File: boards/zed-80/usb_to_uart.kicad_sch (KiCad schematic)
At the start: 11 parts, among them J1 TYPE-C-31-M-12, U1 GD74LS04, U2 CH340C, U6 MC68B50P

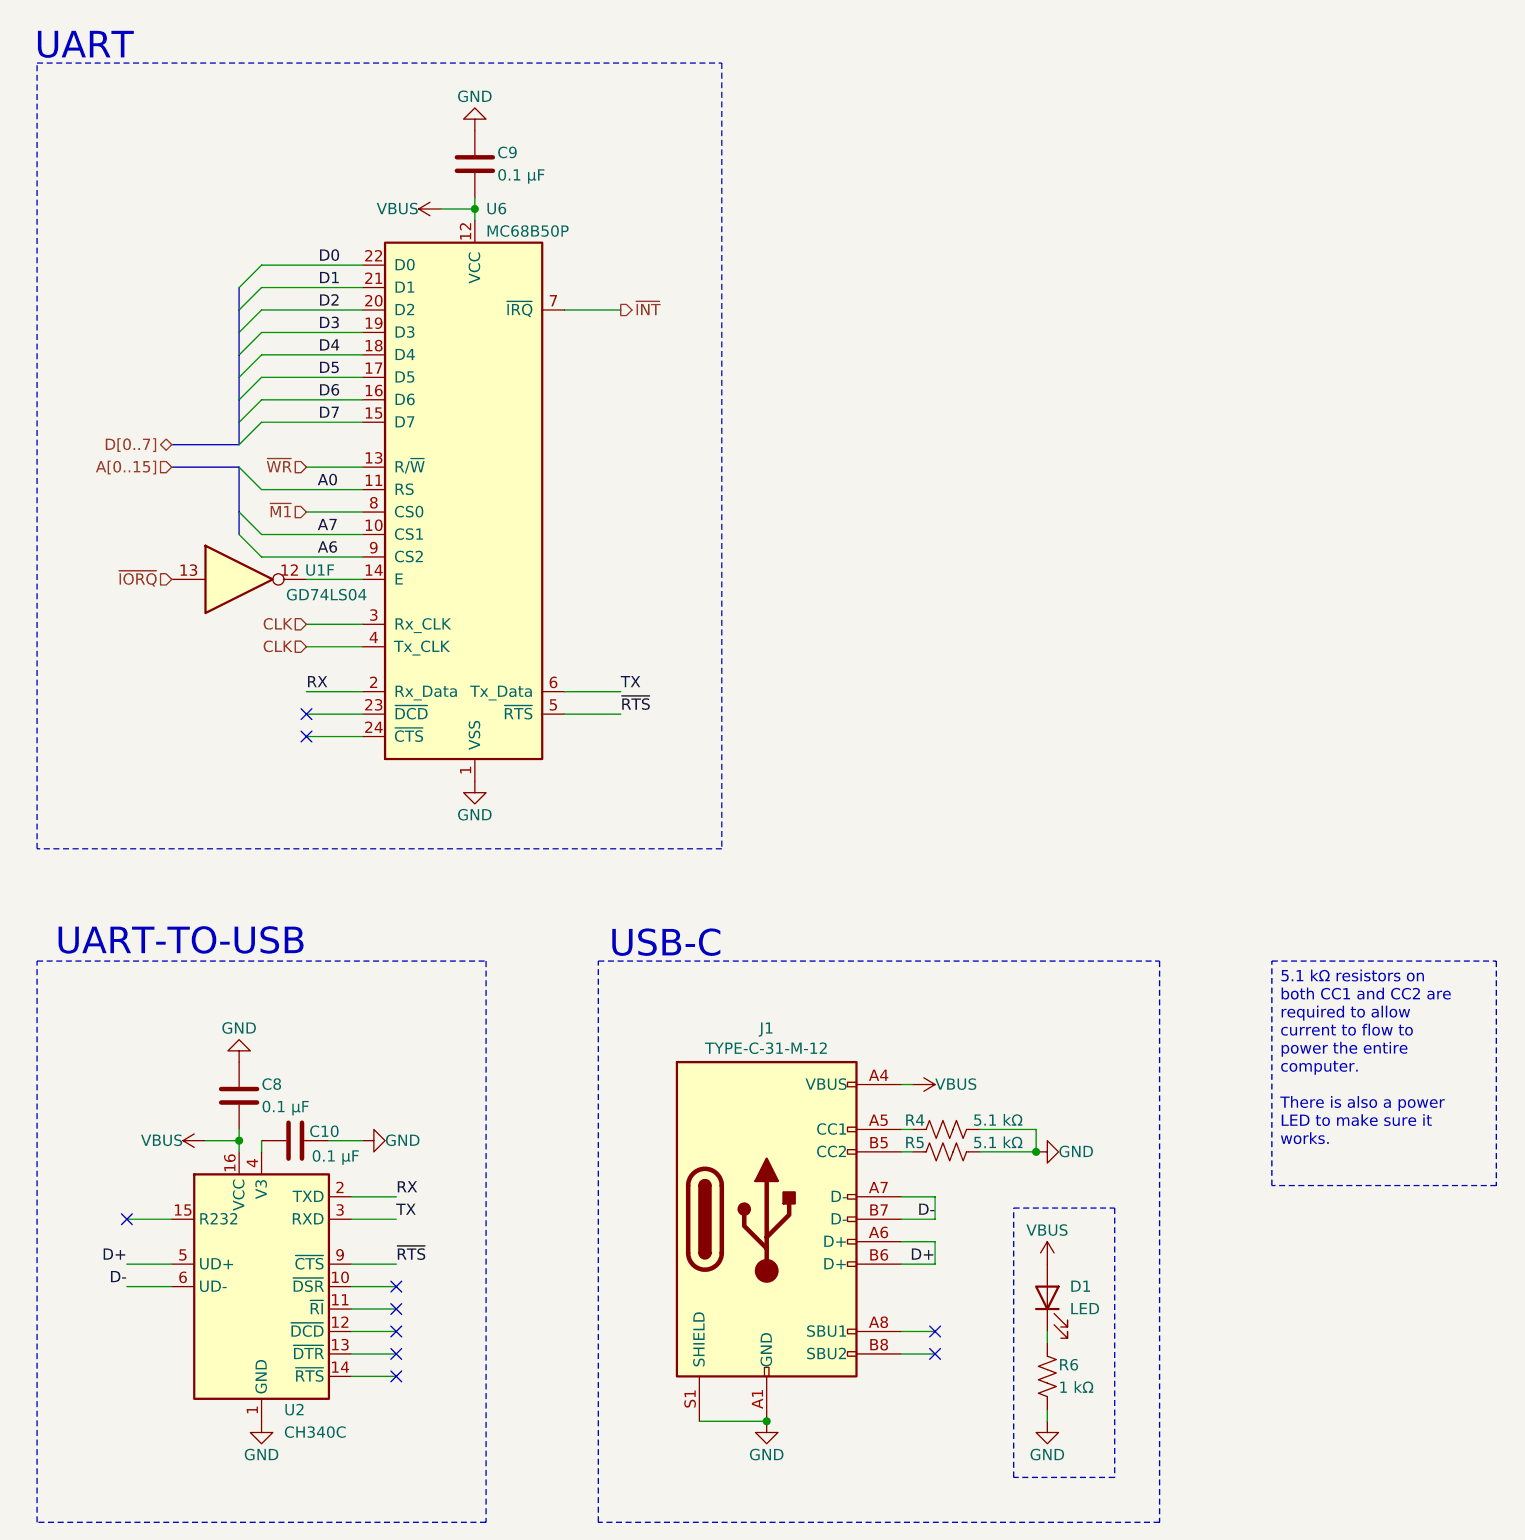
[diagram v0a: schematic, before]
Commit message: Polished schematics and basic PCB setup
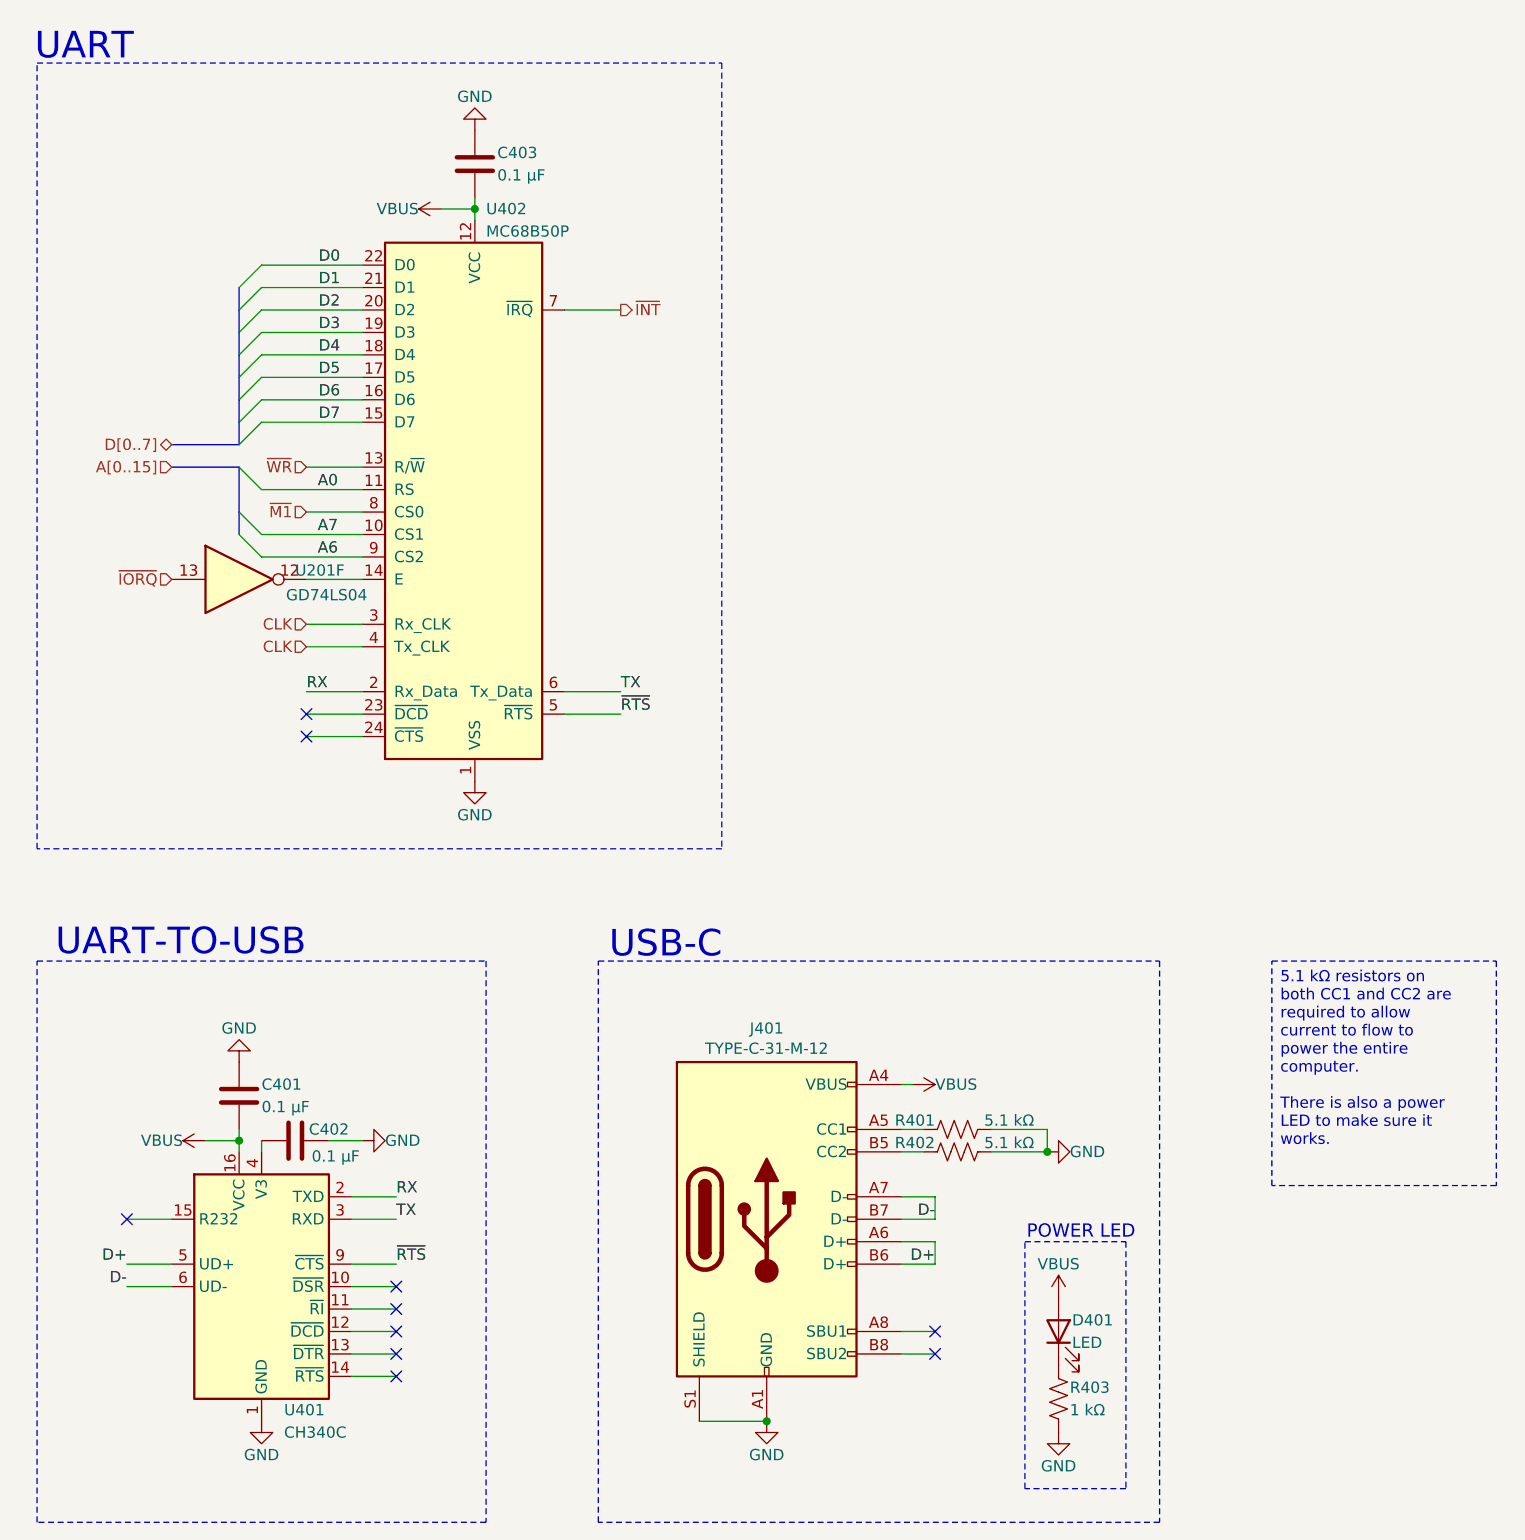
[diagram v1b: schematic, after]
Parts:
- renumbered C8 to C401, C10 to C402, C9 to C403, D1 to D401, J1 to J401, R4 to R401, R5 to R402, R6 to R403, U1 to U201, U2 to U401, U6 to U402
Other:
- note added: "POWER LED"
- company: (none) -> Dragos Bajanica
- title: (none) -> USB-to-UART
- moved on the sheet: D401, R401, R402, R403

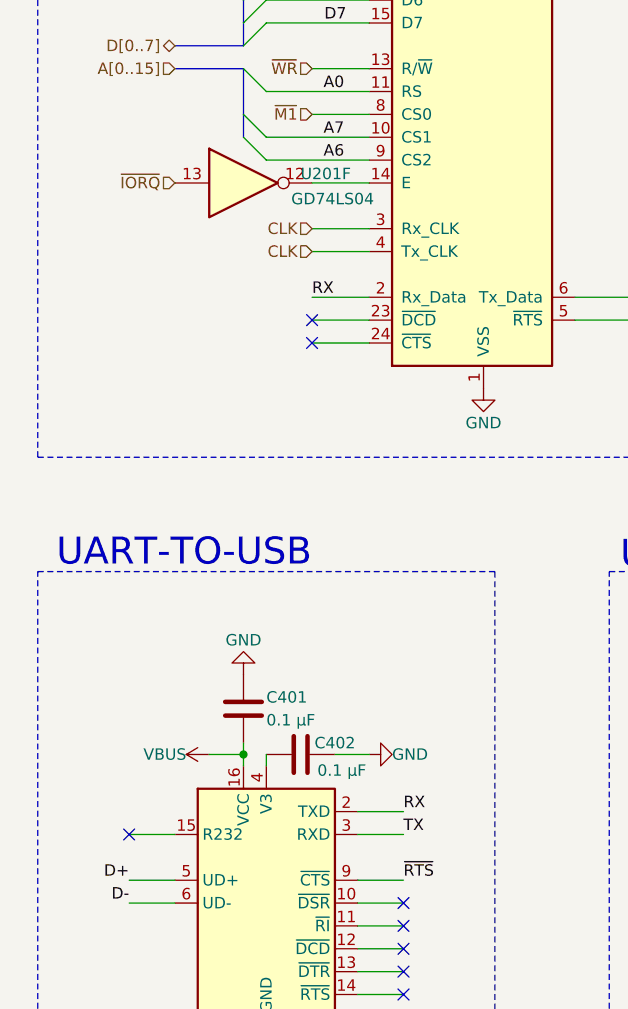
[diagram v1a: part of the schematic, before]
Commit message: New zed-80 revision and initial ROM programmer schematic
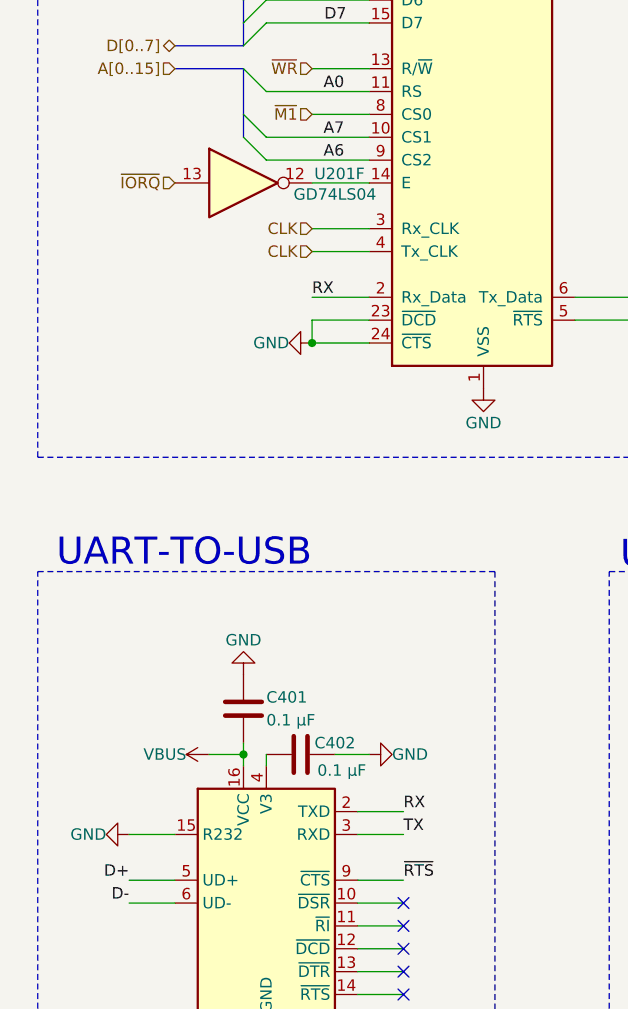
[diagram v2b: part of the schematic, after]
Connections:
- net GND: now also U401.15 (R232), U402.23 (~{DCD}), U402.24 (~{CTS})
- no-connect marks 10 -> 7
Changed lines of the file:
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@@
 	(title_block
 		(title "USB-to-UART")
-		(date "2025-12-31")
-		(rev "A")
+		(date "2026-01-01")
+		(rev "B")
 		(company "Dragos Bajanica")
 	)
@@
 	)
 	(junction
+		(at 55.88 101.6)
+		(diameter 0)
+		(color 0 0 0 0)
+	)
+	(junction
 		(at 107.95 179.07)
 		(diameter 0)
@@
 	)
 	(no_connect
-		(at 55.88 99.06)
-	)
-	(no_connect
 		(at 66.04 168.91)
 	)
@@
 	)
 	(no_connect
-		(at 35.56 156.21)
-	)
-	(no_connect
 		(at 66.04 166.37)
-	)
-	(no_connect
-		(at 55.88 101.6)
 	)
 	(no_connect
@@
 		)
 	)
+	(wire
+		(pts
+			(xy 55.88 99.06) (xy 55.88 101.6)
+		)
+		(stroke
+			(width 0)
+			(type default)
+		)
+	)
 	(bus
 		(pts
@@
 			)
 			(justify left)
+		)
+	)
+	(symbol
+		(lib_id "power:GND")
+		(at 55.88 101.6 270)
+		(mirror x)
+		(unit 1)
+		(exclude_from_sim no)
+		(in_bom yes)
+		(on_board yes)
+		(dnp no)
+		(property "Reference" "#PWR0405"
+			(at 49.53 101.6 0)
+			(effects
+				(font
+					(size 1.27 1.27)
+				)
+				(hide yes)
+			)
+		)
+		(property "Value" "GND"
+			(at 53.34 101.6 90)
+			(effects
+				(font
+					(size 1.27 1.27)
+				)
+				(justify right)
+			)
+		)
+		(property "Footprint" ""
+			(at 55.88 101.6 0)
+			(effects
+				(font
+					(size 1.27 1.27)
+				)
+				(hide yes)
+			)
+		)
+		(property "Datasheet" ""
+			(at 55.88 101.6 0)
+			(effects
+				(font
+					(size 1.27 1.27)
+				)
+				(hide yes)
+			)
+		)
+		(property "Description" "Power symbol creates a global label with name \"GND\" , ground"
+			(at 55.88 101.6 0)
+			(effects
+				(font
+					(size 1.27 1.27)
+				)
+				(hide yes)
+			)
+		)
+		(pin "1"
+		)
+		(instances
+			(project "zed-80"
+				(path "/3141ac47-310a-4fc3-ab78-4d4b51ab76a4/0dd3bd4c-9936-4de5-a023-cfe1468865a6"
+					(reference "#PWR0405")
+					(unit 1)
+				)
+			)
 		)
 	)
@@
 		(on_board yes)
 		(dnp no)
-		(property "Reference" "#PWR0409"
+		(property "Reference" "#PWR0411"
 			(at 120.65 140.97 0)
 			(effects
@@
 			(project "zed-80"
 				(path "/3141ac47-310a-4fc3-ab78-4d4b51ab76a4/0dd3bd4c-9936-4de5-a023-cfe1468865a6"
-					(reference "#PWR0409")
+					(reference "#PWR0411")
 					(unit 1)
 				)
@@
 		(on_board yes)
 		(dnp no)
-		(property "Reference" "#PWR0404"
+		(property "Reference" "#PWR0406"
 			(at 68.58 147.32 0)
 			(effects
@@
 			(project "zed-80"
 				(path "/3141ac47-310a-4fc3-ab78-4d4b51ab76a4/0dd3bd4c-9936-4de5-a023-cfe1468865a6"
-					(reference "#PWR0404")
+					(reference "#PWR0406")
 					(unit 1)
 				)
@@
 		(on_board yes)
 		(dnp no)
-		(property "Reference" "#PWR0401"
+		(property "Reference" "#PWR0402"
 			(at 48.26 147.32 0)
 			(effects
@@
 			(project "zed-80"
 				(path "/3141ac47-310a-4fc3-ab78-4d4b51ab76a4/0dd3bd4c-9936-4de5-a023-cfe1468865a6"
-					(reference "#PWR0401")
+					(reference "#PWR0402")
 					(unit 1)
 				)
@@
 		(on_board yes)
 		(dnp no)
-		(property "Reference" "#PWR0410"
+		(property "Reference" "#PWR0412"
 			(at 146.05 148.59 0)
 			(effects
@@
 			(project "zed-80"
 				(path "/3141ac47-310a-4fc3-ab78-4d4b51ab76a4/0dd3bd4c-9936-4de5-a023-cfe1468865a6"
-					(reference "#PWR0410")
+					(reference "#PWR0412")
 					(unit 1)
 				)
@@
 		(dnp no)
 		(property "Reference" "U201"
-			(at 57.404 82.804 0)
+			(at 58.928 82.804 0)
 			(effects
 				(font
@@
 		)
 		(property "Value" "GD74LS04"
-			(at 58.166 85.598 0)
+			(at 58.42 85.09 0)
 			(effects
 				(font
@@
 		(on_board yes)
 		(dnp no)
-		(property "Reference" "#PWR0403"
+		(property "Reference" "#PWR0404"
 			(at 50.8 185.42 0)
 			(effects
@@
 			(project "zed-80"
 				(path "/3141ac47-310a-4fc3-ab78-4d4b51ab76a4/0dd3bd4c-9936-4de5-a023-cfe1468865a6"
-					(reference "#PWR0403")
+					(reference "#PWR0404")
 					(unit 1)
 				)
@@
 		(on_board yes)
 		(dnp no)
-		(property "Reference" "#PWR0407"
+		(property "Reference" "#PWR0409"
 			(at 74.93 113.03 0)
 			(effects
@@
 			(project "zed-80"
 				(path "/3141ac47-310a-4fc3-ab78-4d4b51ab76a4/0dd3bd4c-9936-4de5-a023-cfe1468865a6"
-					(reference "#PWR0407")
+					(reference "#PWR0409")
 					(unit 1)
 				)
@@
 		(on_board yes)
 		(dnp no)
-		(property "Reference" "#PWR0402"
+		(property "Reference" "#PWR0403"
 			(at 48.26 132.08 0)
 			(effects
@@
 			(project "zed-80"
 				(path "/3141ac47-310a-4fc3-ab78-4d4b51ab76a4/0dd3bd4c-9936-4de5-a023-cfe1468865a6"
-					(reference "#PWR0402")
+					(reference "#PWR0403")
 					(unit 1)
 				)
@@
 		(on_board yes)
 		(dnp no)
-		(property "Reference" "#PWR0412"
+		(property "Reference" "#PWR0414"
 			(at 140.97 186.69 0)
 			(effects
@@
 			(project "zed-80"
 				(path "/3141ac47-310a-4fc3-ab78-4d4b51ab76a4/0dd3bd4c-9936-4de5-a023-cfe1468865a6"
-					(reference "#PWR0412")
+					(reference "#PWR0414")
 					(unit 1)
 				)
@@
 		(on_board yes)
 		(dnp no)
-		(property "Reference" "#PWR0411"
+		(property "Reference" "#PWR0413"
 			(at 140.97 168.91 0)
 			(effects
@@
 			(project ""
 				(path "/3141ac47-310a-4fc3-ab78-4d4b51ab76a4/0dd3bd4c-9936-4de5-a023-cfe1468865a6"
-					(reference "#PWR0411")
+					(reference "#PWR0413")
 					(unit 1)
 				)
@@
 		(on_board yes)
 		(dnp no)
-		(property "Reference" "#PWR0408"
+		(property "Reference" "#PWR0410"
 			(at 107.95 185.42 0)
 			(effects
@@
 			(project "zed-80"
 				(path "/3141ac47-310a-4fc3-ab78-4d4b51ab76a4/0dd3bd4c-9936-4de5-a023-cfe1468865a6"
-					(reference "#PWR0408")
+					(reference "#PWR0410")
 					(unit 1)
 				)
@@
 		(on_board yes)
 		(dnp no)
-		(property "Reference" "#PWR0405"
+		(property "Reference" "#PWR0407"
 			(at 74.93 41.91 0)
 			(effects
@@
 			(project "zed-80"
 				(path "/3141ac47-310a-4fc3-ab78-4d4b51ab76a4/0dd3bd4c-9936-4de5-a023-cfe1468865a6"
-					(reference "#PWR0405")
+					(reference "#PWR0407")
 					(unit 1)
 				)
@@
 		(on_board yes)
 		(dnp no)
-		(property "Reference" "#PWR0406"
+		(property "Reference" "#PWR0408"
 			(at 74.93 26.67 0)
 			(effects
@@
 			(project "zed-80"
 				(path "/3141ac47-310a-4fc3-ab78-4d4b51ab76a4/0dd3bd4c-9936-4de5-a023-cfe1468865a6"
-					(reference "#PWR0406")
+					(reference "#PWR0408")
 					(unit 1)
 				)
+			)
+		)
+	)
+	(symbol
+		(lib_id "power:GND")
+		(at 35.56 156.21 270)
+		(mirror x)
+		(unit 1)
+		(exclude_from_sim no)
+		(in_bom yes)
+		(on_board yes)
+		(dnp no)
+		(property "Reference" "#PWR0401"
+			(at 29.21 156.21 0)
+			(effects
+				(font
+					(size 1.27 1.27)
+				)
+				(hide yes)
+			)
+		)
+		(property "Value" "GND"
+			(at 33.02 156.21 90)
+			(effects
+				(font
+					(size 1.27 1.27)
+				)
+				(justify right)
+			)
+		)
+		(property "Footprint" ""
+			(at 35.56 156.21 0)
+			(effects
+				(font
+					(size 1.27 1.27)
+				)
+				(hide yes)
+			)
+		)
+		(property "Datasheet" ""
+			(at 35.56 156.21 0)
+			(effects
+				(font
+					(size 1.27 1.27)
+				)
+				(hide yes)
+			)
+		)
+		(property "Description" "Power symbol creates a global label with name \"GND\" , ground"
+			(at 35.56 156.21 0)
+			(effects
+				(font
+					(size 1.27 1.27)
+				)
+				(hide yes)
+			)
+		)
+		(pin "1"
+		)
+		(instances
+			(project "zed-80"
+				(path "/3141ac47-310a-4fc3-ab78-4d4b51ab76a4/0dd3bd4c-9936-4de5-a023-cfe1468865a6"
+					(reference "#PWR0401")
+					(unit 1)
+				)

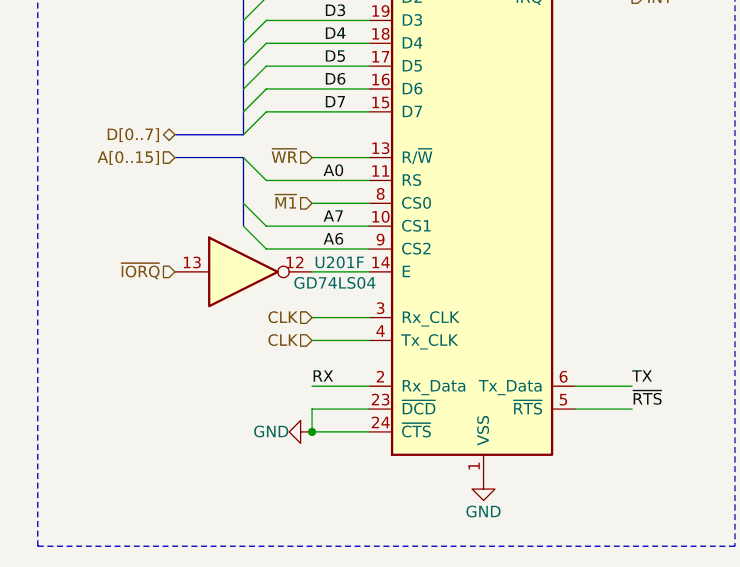
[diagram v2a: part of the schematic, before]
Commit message: Fixed clock oscillator circuit
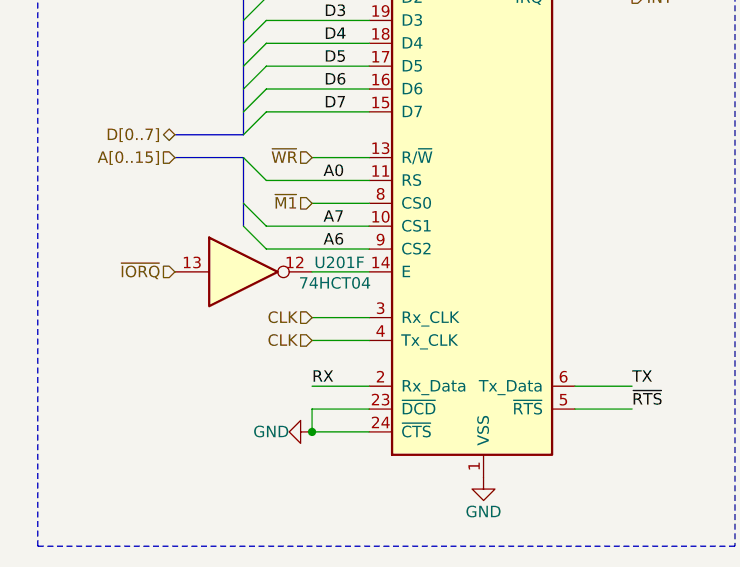
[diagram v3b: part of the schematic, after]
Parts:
- U201: value GD74LS04 -> 74HCT04
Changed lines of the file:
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@@
 	(title_block
 		(title "USB-to-UART")
-		(date "2026-01-01")
-		(rev "B")
+		(date "2026-03-17")
+		(rev "C")
 		(company "Dragos Bajanica")
 	)
@@
 		)
 		(instances
-			(project ""
+			(project "zed-80"
 				(path "/3141ac47-310a-4fc3-ab78-4d4b51ab76a4/0dd3bd4c-9936-4de5-a023-cfe1468865a6"
 					(reference "D401")
@@
 			)
 		)
-		(property "Value" "GD74LS04"
+		(property "Value" "74HCT04"
 			(at 58.42 85.09 0)
 			(effects
@@
 		)
 		(instances
-			(project ""
+			(project "zed-80"
 				(path "/3141ac47-310a-4fc3-ab78-4d4b51ab76a4/0dd3bd4c-9936-4de5-a023-cfe1468865a6"
 					(reference "#PWR0413")
